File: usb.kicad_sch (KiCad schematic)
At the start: 28 parts, among them J2 USB4105, J3 USB-A-S-F-B-VU, U1 MX6UL-VM, U11 TPD4EUSB30, U12 74LVC1G04, U13 D5V0H1B2LP, U4 TUSB320, U5 AP22811B, U6 TPD4EUSB30, U7 D5V0H1B2LP

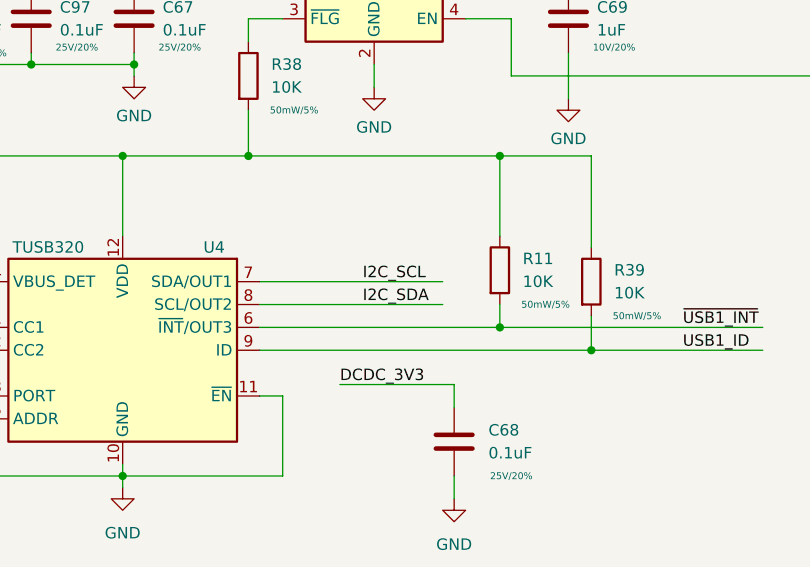
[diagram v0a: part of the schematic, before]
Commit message: tusb320: fix swaped SDA/SCL
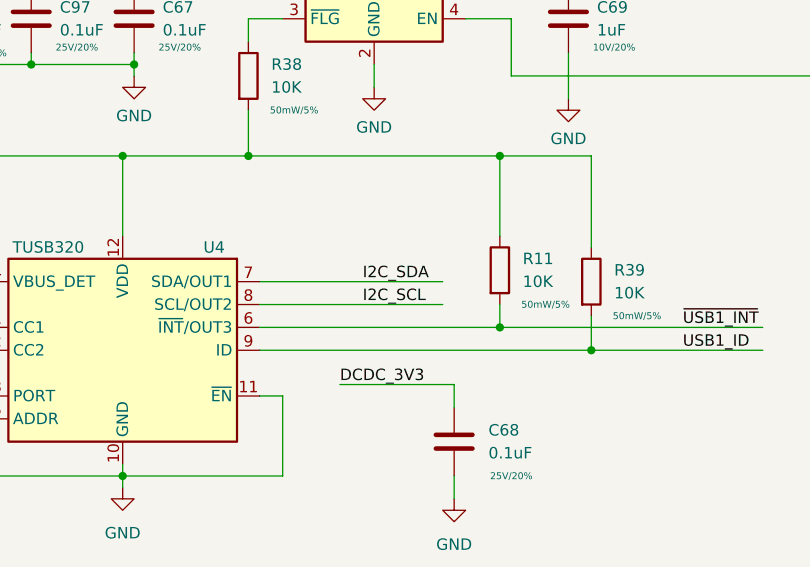
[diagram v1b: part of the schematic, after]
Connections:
- net I2C_SCL: now also U4.8 (SCL/OUT2); no longer U4.7 (SDA/OUT1)
- net I2C_SDA: now also U4.7 (SDA/OUT1); no longer U4.8 (SCL/OUT2)
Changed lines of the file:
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@@
     (effects (font (size 1.27 1.27)) (justify left bottom))
   )
-  (label "I2C_SDA" (at 193.04 163.83 0)
+  (label "I2C_SDA" (at 193.04 161.29 0)
     (effects (font (size 1.27 1.27)) (justify left bottom))
   )
@@
     (effects (font (size 1.27 1.27)) (justify left bottom))
   )
-  (label "I2C_SCL" (at 193.04 161.29 0)
+  (label "I2C_SCL" (at 193.04 163.83 0)
     (effects (font (size 1.27 1.27)) (justify left bottom))
   )

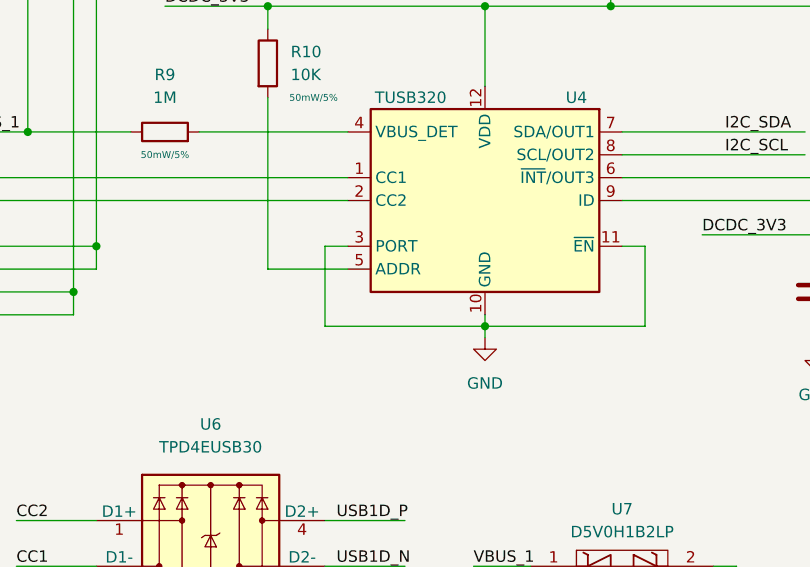
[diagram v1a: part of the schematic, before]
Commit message: tusb320: use drp mode
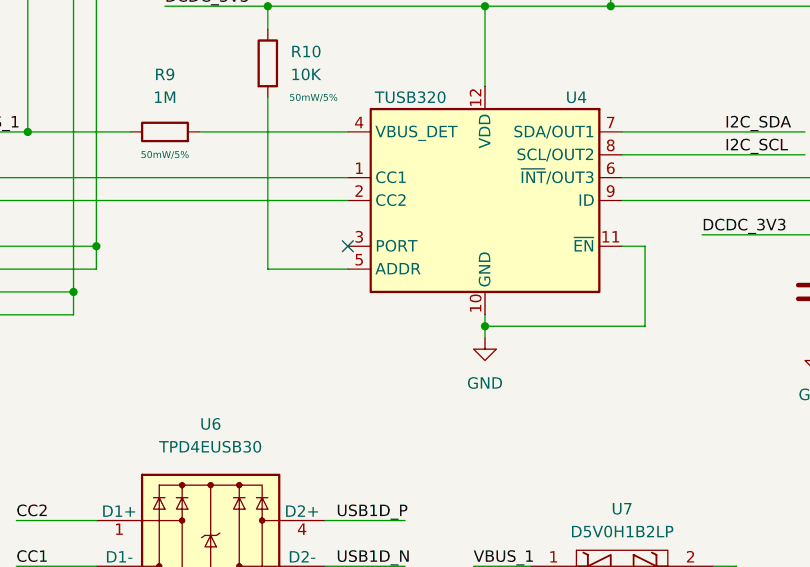
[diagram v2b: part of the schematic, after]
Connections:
- net GND: no longer U4.3 (PORT)
- no-connect marks 5 -> 6
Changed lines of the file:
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@@
   (junction (at 254 66.04) (diameter 0) (color 0 0 0 0)
   )
+  (no_connect (at 151.13 173.99))
   (no_connect (at 228.6 88.9))
   (no_connect (at 228.6 83.82))
@@
     (stroke (width 0) (type default) (color 0 0 0 0))
   )
-  (wire (pts (xy 151.13 173.99) (xy 148.59 173.99))
-    (stroke (width 0) (type default) (color 0 0 0 0))
-  )
-  (wire (pts (xy 148.59 182.88) (xy 166.37 182.88))
-    (stroke (width 0) (type default) (color 0 0 0 0))
-  )
-  (wire (pts (xy 148.59 173.99) (xy 148.59 182.88))
-    (stroke (width 0) (type default) (color 0 0 0 0))
-  )
